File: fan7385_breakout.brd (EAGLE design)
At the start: 28.6 x 14 mm, 15 parts

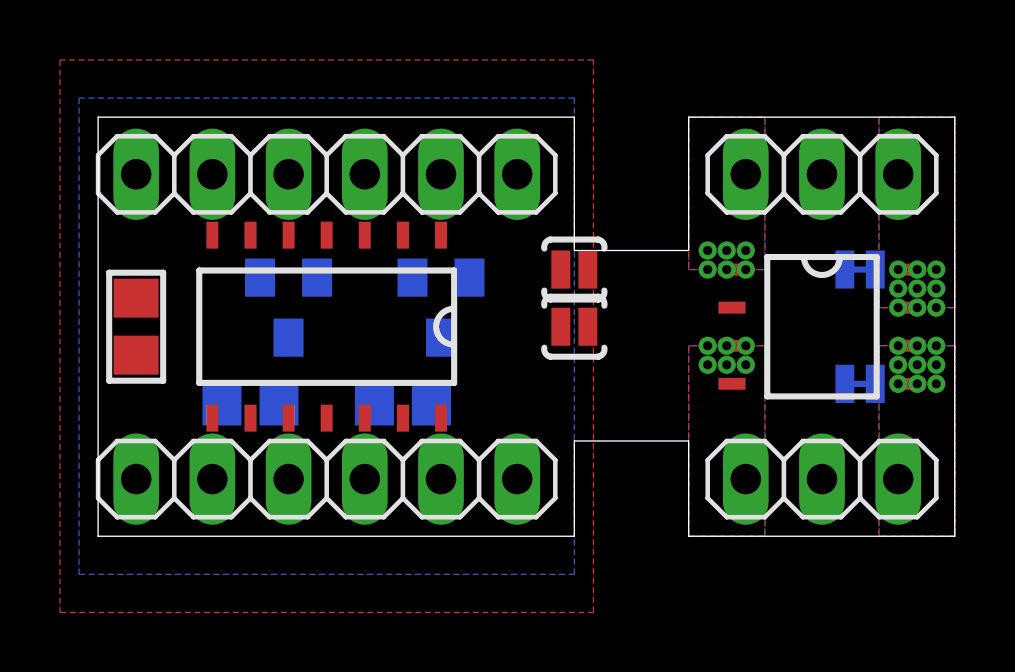
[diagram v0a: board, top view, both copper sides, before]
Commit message: a bit of manual routing, hoping it will help
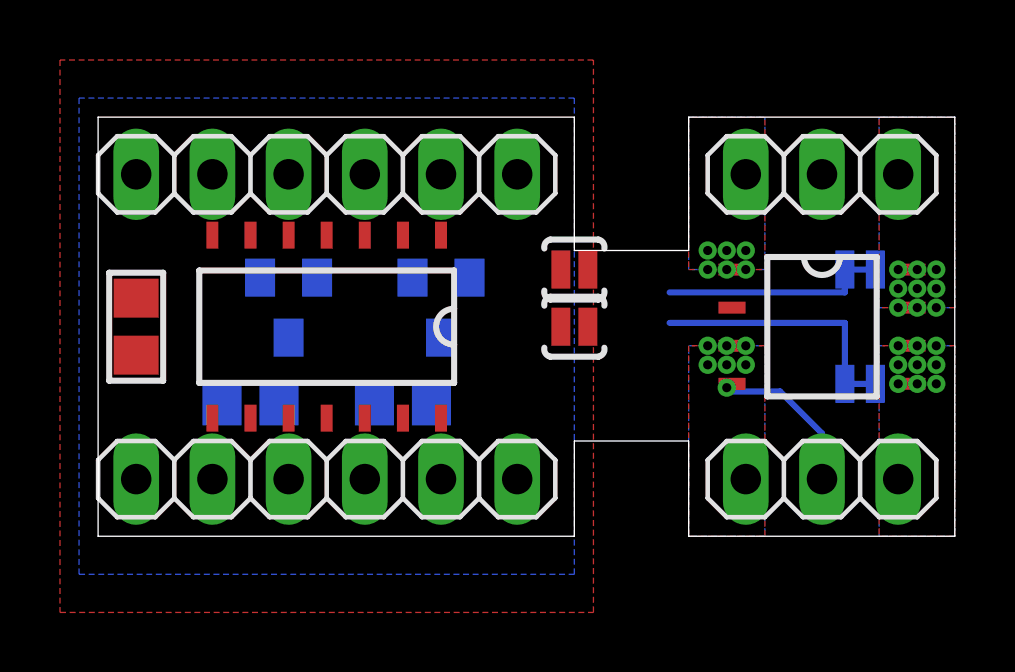
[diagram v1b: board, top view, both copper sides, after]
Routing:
- net VS2: track 0.00 -> 7.87 mm
- net VS1: track 0.00 -> 6.60 mm
- net HO2/G2: track 0.00 -> 5.56 mm, vias 0 -> 1
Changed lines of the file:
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@@
 <setting verticaltext="up"/>
 </settings>
-<grid distance="25" unitdist="mil" unit="mil" style="lines" multiple="1" display="yes" altdistance="0.025" altunitdist="inch" altunit="inch"/>
+<grid distance="5" unitdist="mil" unit="mil" style="lines" multiple="1" display="yes" altdistance="0.025" altunitdist="inch" altunit="inch"/>
 <layers>
 <layer number="1" name="Top" color="4" fill="1" visible="yes" active="yes"/>
@@
 <contactref element="JP2" pad="2"/>
 <contactref element="JP3" pad="2"/>
-<wire x1="24.13" y1="1.905" x2="21.13" y2="5.08" width="0" layer="19" extent="1-1"/>
-<wire x1="5.08" y1="3.935" x2="21.13" y2="5.08" width="0" layer="19" extent="1-1"/>
+<via x="20.955" y="4.953" extent="1-16" drill="0.3048" shape="square"/>
+<wire x1="24.13" y1="1.905" x2="24.13" y2="3.429" width="0.2032" layer="16"/>
+<wire x1="24.13" y1="3.429" x2="22.733" y2="4.826" width="0.2032" layer="16"/>
+<wire x1="22.733" y1="4.826" x2="21.082" y2="4.826" width="0.2032" layer="16"/>
+<wire x1="21.082" y1="4.826" x2="20.955" y2="4.953" width="0.2032" layer="16"/>
+<wire x1="21.13" y1="5.08" x2="21.082" y2="5.08" width="0.2032" layer="1"/>
+<wire x1="21.082" y1="5.08" x2="20.955" y2="4.953" width="0.2032" layer="1"/>
+<wire x1="5.08" y1="3.935" x2="20.955" y2="4.953" width="0" layer="19" extent="1-16"/>
 <wire x1="3.81" y1="1.905" x2="5.08" y2="3.935" width="0" layer="19" extent="1-1"/>
 </signal>
@@
 <contactref element="JP2" pad="4"/>
 <contactref element="CBOOT1" pad="1"/>
-<wire x1="9.21" y1="4.445" x2="24.892" y2="8.89" width="0" layer="19" extent="16-16"/>
+<wire x1="24.892" y1="8.89" x2="24.892" y2="8.128" width="0.2032" layer="16"/>
+<wire x1="24.892" y1="8.128" x2="19.05" y2="8.128" width="0.2032" layer="16"/>
+<wire x1="9.21" y1="4.445" x2="19.05" y2="8.128" width="0" layer="19" extent="16-16"/>
 <wire x1="8.89" y1="3.935" x2="9.21" y2="4.445" width="0" layer="19" extent="1-16"/>
 <wire x1="8.89" y1="1.905" x2="8.89" y2="3.935" width="0" layer="19" extent="1-1"/>
@@
 <contactref element="JP2" pad="1"/>
 <contactref element="CBOOT2" pad="1"/>
-<wire x1="4.13" y1="4.445" x2="24.892" y2="5.08" width="0" layer="19" extent="16-16"/>
+<wire x1="24.892" y1="5.08" x2="24.892" y2="7.112" width="0.2032" layer="16"/>
+<wire x1="24.892" y1="7.112" x2="19.05" y2="7.112" width="0.2032" layer="16"/>
+<wire x1="4.13" y1="4.445" x2="19.05" y2="7.112" width="0" layer="19" extent="16-16"/>
 <wire x1="3.81" y1="3.935" x2="4.13" y2="4.445" width="0" layer="19" extent="1-16"/>
 <wire x1="1.27" y1="1.905" x2="3.81" y2="3.935" width="0" layer="19" extent="1-1"/>

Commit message: switched to octagon pads to solve a clearance issue
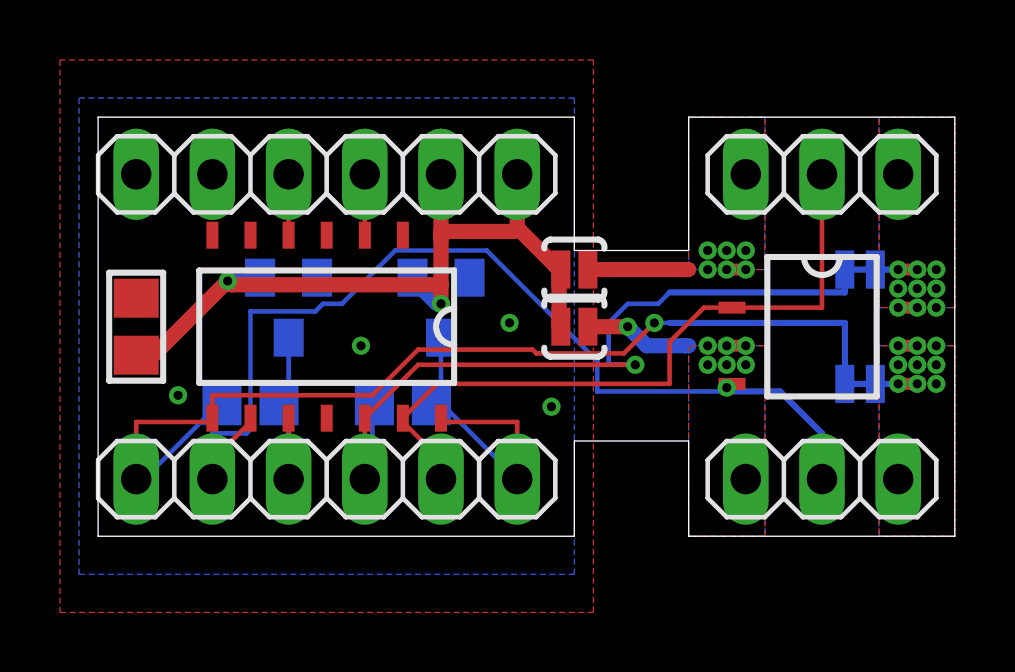
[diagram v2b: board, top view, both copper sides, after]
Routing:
- net HO2/G2: track 5.56 -> 34.3 mm
- net VDD: track 0.00 -> 26.5 mm, vias 0 -> 2
- net VS2: track 7.87 -> 33.5 mm, vias 0 -> 1
- net HO1/G1: track 0.00 -> 23.3 mm
- net VS1: track 6.60 -> 26.0 mm, vias 0 -> 1
- net VB1: track 0.00 -> 11.0 mm
- net VB2: track 0.00 -> 7.38 mm
- net S2: track 0.00 -> 3.62 mm, vias 6 -> 7
- net S1: track 0.00 -> 3.36 mm
- net IN2: track 0.00 -> 2.03 mm
- net IN1: track 0.00 -> 2.03 mm
- net D2: track 0.00 -> 0.76 mm
- net D1: track 0.00 -> 0.76 mm

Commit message: route some more stuff manually first, adjust shape for symmetry
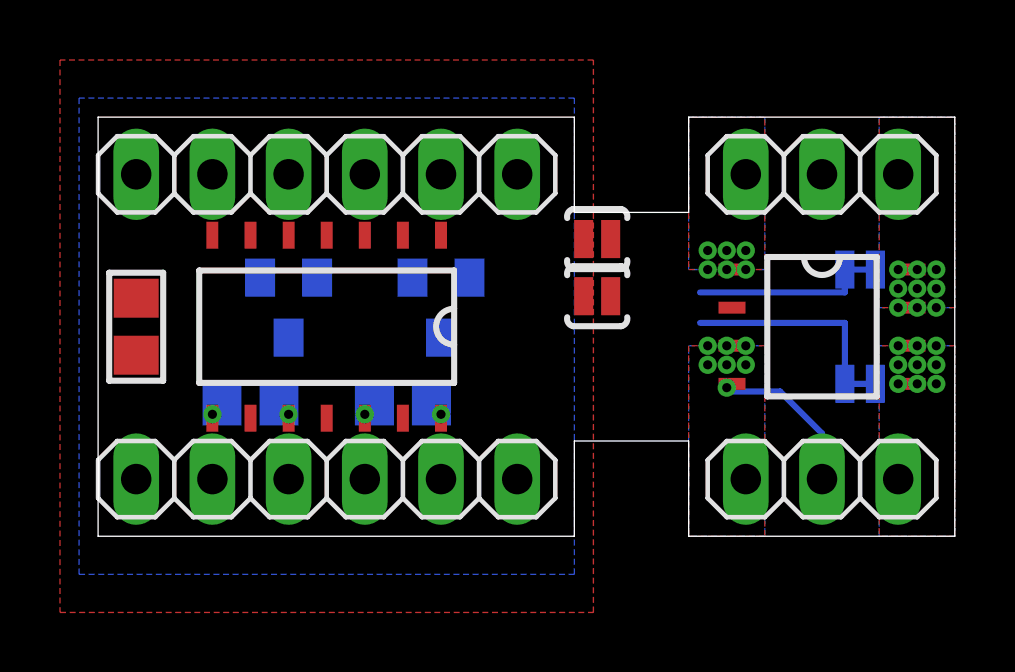
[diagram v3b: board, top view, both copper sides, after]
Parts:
- moved SJ2 1.27 mm to (16.6, 9.91)
- moved SJ1 1.27 mm to (16.6, 8.00)
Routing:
- net HO2/G2: track 34.3 -> 5.56 mm
- net VS2: track 33.5 -> 6.86 mm
- net VDD: track 26.5 -> 0.00 mm, vias 2 -> 0
- net HO1/G1: track 23.3 -> 0.00 mm
- net VS1: track 26.0 -> 5.59 mm
- net VB1: track 11.0 -> 0.00 mm, vias 0 -> 1
- net VB2: track 7.38 -> 0.00 mm, vias 0 -> 1
- net S2: track 3.62 -> 0.00 mm, vias 7 -> 6
- net S1: track 3.36 -> 0.00 mm
- net IN2: track 2.03 -> 0.00 mm
- net IN1: track 2.03 -> 0.00 mm
- net D2: track 0.76 -> 0.00 mm
- net D1: track 0.76 -> 0.00 mm
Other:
- outline, holes or cut-outs redrawn

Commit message: diffeent pin header part and 100mil spacing between pins
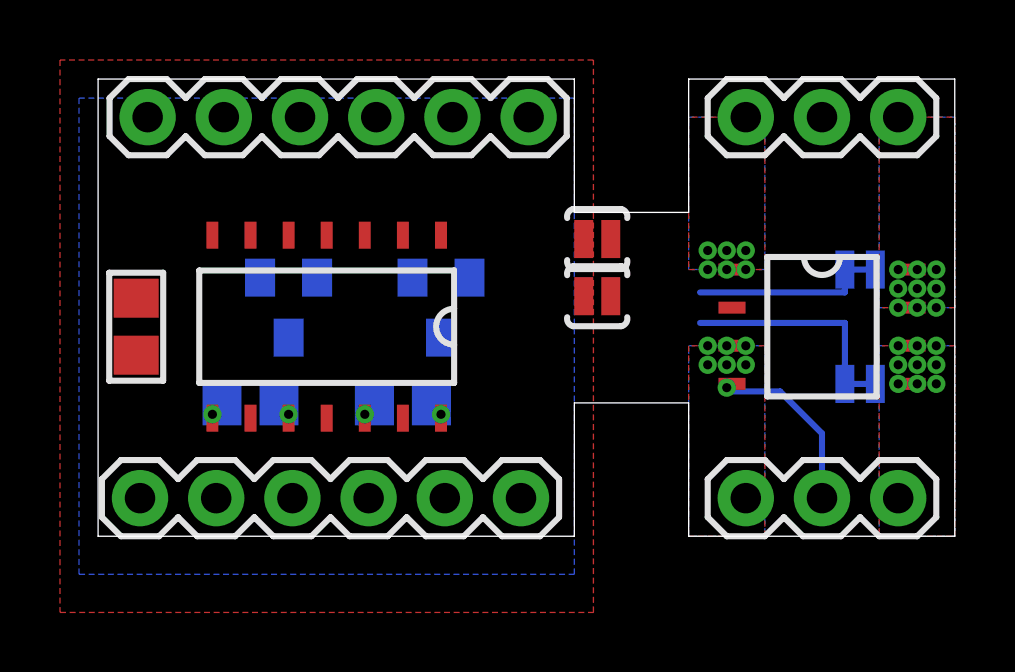
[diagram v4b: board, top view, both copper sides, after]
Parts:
- JP1, JP2: device pinhead:1X06 -> SparkFun-Connectors:1X06
- JP3, JP4: device pinhead:1X03 -> SparkFun-Connectors:1X03
- moved JP1 6.27 mm to (1.65, 14.0)
- moved JP2 6.26 mm to (1.40, 1.27)
- moved JP4 3.18 mm to (21.6, 14.0)
- moved JP3 2.62 mm to (21.6, 1.27)
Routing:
- net HO2/G2: track 5.56 -> 6.19 mm
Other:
- board size 28.6 x 14 mm -> 28.6 x 15.2 mm

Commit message: moved parts around a bit, put the bypass cap to gnd using vias
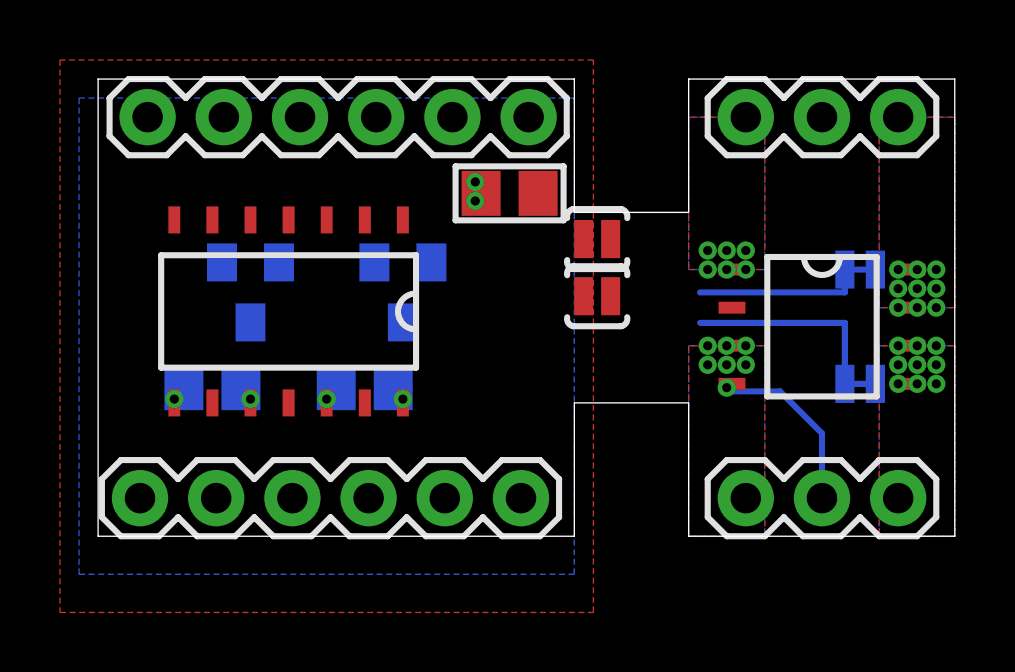
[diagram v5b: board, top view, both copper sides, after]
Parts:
- moved CVDD 13.2 mm to (13.7, 11.4), turned to 0 degrees
- moved GATEDRV 1.37 mm to (6.35, 7.49)
- moved CBOOT2 1.37 mm to (3.81, 4.95)
- moved CBOOT1 1.37 mm to (8.89, 4.95)
- moved DBOOT1 1.37 mm to (10.2, 8.13)
- moved DBOOT2 1.37 mm to (5.08, 8.13)
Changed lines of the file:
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@@
 <setting verticaltext="up"/>
 </settings>
-<grid distance="50" unitdist="mil" unit="mil" style="lines" multiple="1" display="yes" altdistance="0.025" altunitdist="inch" altunit="inch"/>
+<grid distance="5" unitdist="mil" unit="mil" style="lines" multiple="1" display="yes" altdistance="0.025" altunitdist="inch" altunit="inch"/>
 <layers>
 <layer number="1" name="Top" color="4" fill="1" visible="yes" active="yes"/>
@@
 </autorouter>
 <elements>
-<element name="GATEDRV" library="fan7385" package="SOT14" value="FAN7385" x="7.62" y="6.985" smashed="yes" rot="R270"/>
+<element name="GATEDRV" library="fan7385" package="SOT14" value="FAN7385" x="6.35" y="7.493" smashed="yes" rot="R270"/>
 <element name="FET" library="DMG9926" package="SOP8-L" value="DMG9926" x="24.13" y="6.985" smashed="yes"/>
-<element name="CBOOT1" library="microbuilder" package="0805" value="0.1uF 25V" x="10.16" y="4.445" smashed="yes" rot="MR180"/>
-<element name="CBOOT2" library="microbuilder" package="0805" value="0.1uF 25V" x="5.08" y="4.445" smashed="yes" rot="MR180"/>
-<element name="CVDD" library="microbuilder" package="0805" value="0.1uF 25V" x="1.27" y="6.985" smashed="yes" rot="R270"/>
-<element name="DBOOT2" library="microbuilder" package="SOT23-WIDE" value="" x="6.35" y="7.62" smashed="yes" rot="MR180">
-<attribute name="VALUE" x="8.255" y="8.255" size="0.4064" layer="28" ratio="10" rot="MR180"/>
+<element name="CBOOT1" library="microbuilder" package="0805" value="0.1uF 25V" x="8.89" y="4.953" smashed="yes" rot="MR180"/>
+<element name="CBOOT2" library="microbuilder" package="0805" value="0.1uF 25V" x="3.81" y="4.953" smashed="yes" rot="MR180"/>
+<element name="CVDD" library="microbuilder" package="0805" value="0.1uF 25V" x="13.716" y="11.43" smashed="yes"/>
+<element name="DBOOT2" library="microbuilder" package="SOT23-WIDE" value="" x="5.08" y="8.128" smashed="yes" rot="MR180">
+<attribute name="VALUE" x="6.985" y="8.763" size="0.4064" layer="28" ratio="10" rot="MR180"/>
 </element>
-<element name="DBOOT1" library="microbuilder" package="SOT23-WIDE" value="" x="11.43" y="7.62" smashed="yes" rot="MR180">
-<attribute name="VALUE" x="13.335" y="8.255" size="0.4064" layer="28" ratio="10" rot="MR180"/>
+<element name="DBOOT1" library="microbuilder" package="SOT23-WIDE" value="" x="10.16" y="8.128" smashed="yes" rot="MR180">
+<attribute name="VALUE" x="12.065" y="8.763" size="0.4064" layer="28" ratio="10" rot="MR180"/>
 </element>
 <element name="SJ1" library="SparkFun-Passives" package="SJ_2S-NO" value="SOLDERJUMPERNO" x="16.637" y="8.001" smashed="yes"/>
@@
 <contactref element="JP1" pad="2"/>
 <contactref element="JP1" pad="1"/>
+<via x="12.573" y="11.811" extent="1-16" drill="0.3048" shape="square"/>
+<via x="12.573" y="11.176" extent="1-16" drill="0.3048" shape="square"/>
 </signal>
 <signal name="VDD" class="2">
@@
 <contactref element="JP1" pad="6"/>
 <contactref element="JP1" pad="5"/>
+<wire x1="14.666" y1="11.43" x2="14.351" y2="13.97" width="0" layer="19" extent="1-1"/>
+<wire x1="16.187" y1="9.906" x2="14.666" y2="11.43" width="0" layer="19" extent="1-1"/>
+<wire x1="16.187" y1="8.001" x2="16.187" y2="9.906" width="0" layer="19" extent="1-1"/>
 <wire x1="11.811" y1="13.97" x2="14.351" y2="13.97" width="0" layer="19" extent="1-1"/>
-<wire x1="11.43" y1="10.035" x2="11.811" y2="13.97" width="0" layer="19" extent="1-1"/>
-<wire x1="10.48" y1="8.62" x2="11.43" y2="10.035" width="0" layer="19" extent="1-16"/>
-<wire x1="16.187" y1="9.906" x2="14.351" y2="13.97" width="0" layer="19" extent="1-1"/>
-<wire x1="16.187" y1="8.001" x2="16.187" y2="9.906" width="0" layer="19" extent="1-1"/>
-<wire x1="5.4" y1="8.62" x2="10.48" y2="8.62" width="0" layer="19" extent="16-16"/>
-<wire x1="1.27" y1="6.035" x2="5.4" y2="8.62" width="0" layer="19" extent="1-16"/>
+<wire x1="10.16" y1="10.543" x2="11.811" y2="13.97" width="0" layer="19" extent="1-1"/>
+<wire x1="9.21" y1="9.128" x2="10.16" y2="10.543" width="0" layer="19" extent="1-16"/>
+<wire x1="4.13" y1="9.128" x2="9.21" y2="9.128" width="0" layer="19" extent="16-16"/>
 </signal>
 <signal name="S1" class="2">
@@
 <contactref element="GATEDRV" pad="3"/>
 <contactref element="JP1" pad="4"/>
-<wire x1="8.89" y1="10.035" x2="9.271" y2="13.97" width="0" layer="19" extent="1-1"/>
+<wire x1="7.62" y1="10.543" x2="9.271" y2="13.97" width="0" layer="19" extent="1-1"/>
 </signal>
 <signal name="IN2">
 <contactref element="GATEDRV" pad="5"/>
 <contactref element="JP1" pad="3"/>
-<wire x1="6.35" y1="10.035" x2="6.731" y2="13.97" width="0" layer="19" extent="1-1"/>
+<wire x1="5.08" y1="10.543" x2="6.731" y2="13.97" width="0" layer="19" extent="1-1"/>
 </signal>
 <signal name="HO1/G1">
@@
 <wire x1="21.13" y1="7.62" x2="24.13" y2="13.97" width="0" layer="19" extent="1-1"/>
 <wire x1="11.557" y1="1.27" x2="21.13" y2="7.62" width="0" layer="19" extent="1-1"/>
-<wire x1="10.16" y1="3.935" x2="11.557" y2="1.27" width="0" layer="19" extent="1-1"/>
+<wire x1="8.89" y1="4.443" x2="11.557" y2="1.27" width="0" layer="19" extent="1-1"/>
 </signal>
 <signal name="HO2/G2">
@@
 <contactref element="JP2" pad="2"/>
 <contactref element="JP3" pad="2"/>
-<wire x1="5.08" y1="3.935" x2="20.955" y2="4.953" width="0" layer="19" extent="1-16"/>
-<wire x1="3.937" y1="1.27" x2="5.08" y2="3.935" width="0" layer="19" extent="1-1"/>
 <wire x1="24.13" y1="3.429" x2="24.13" y2="1.27" width="0.2032" layer="16"/>
+<wire x1="3.81" y1="4.443" x2="20.955" y2="4.953" width="0" layer="19" extent="1-1"/>
+<wire x1="3.937" y1="1.27" x2="3.81" y2="4.443" width="0" layer="19" extent="1-1"/>
 </signal>
 <signal name="VB1">
@@
 <contactref element="CBOOT1" pad="2"/>
 <contactref element="DBOOT1" pad="3"/>
-<via x="11.43" y="4.064" extent="1-16" drill="0.3048" shape="square"/>
+<via x="10.16" y="4.572" extent="1-16" drill="0.3048" shape="square"/>
 <contactref element="JP2" pad="6"/>
-<wire x1="11.11" y1="4.445" x2="11.43" y2="6.62" width="0" layer="19" extent="16-16"/>
-<wire x1="11.43" y1="4.064" x2="11.11" y2="4.445" width="0" layer="19" extent="16-16"/>
-<wire x1="11.43" y1="3.935" x2="11.43" y2="4.064" width="0" layer="19" extent="1-1"/>
-<wire x1="14.097" y1="1.27" x2="11.43" y2="3.935" width="0" layer="19" extent="1-1"/>
+<wire x1="9.84" y1="4.953" x2="10.16" y2="7.128" width="0" layer="19" extent="16-16"/>
+<wire x1="10.16" y1="4.572" x2="9.84" y2="4.953" width="0" layer="19" extent="16-16"/>
+<wire x1="10.16" y1="4.443" x2="10.16" y2="4.572" width="0" layer="19" extent="1-1"/>
+<wire x1="14.097" y1="1.27" x2="10.16" y2="4.443" width="0" layer="19" extent="1-1"/>
 </signal>
 <signal name="VB2">
@@
 <contactref element="CBOOT2" pad="2"/>
 <contactref element="DBOOT2" pad="3"/>
-<via x="6.35" y="4.064" extent="1-16" drill="0.3048" shape="square"/>
+<via x="5.08" y="4.572" extent="1-16" drill="0.3048" shape="square"/>
 <contactref element="JP2" pad="3"/>
-<wire x1="6.03" y1="4.445" x2="6.35" y2="6.62" width="0" layer="19" extent="16-16"/>
-<wire x1="6.35" y1="4.064" x2="6.03" y2="4.445" width="0" layer="19" extent="16-16"/>
-<wire x1="6.35" y1="3.935" x2="6.35" y2="4.064" width="0" layer="19" extent="1-1"/>
-<wire x1="6.477" y1="1.27" x2="6.35" y2="3.935" width="0" layer="19" extent="1-1"/>
+<wire x1="4.76" y1="4.953" x2="5.08" y2="7.128" width="0" layer="19" extent="16-16"/>
+<wire x1="5.08" y1="4.572" x2="4.76" y2="4.953" width="0" layer="19" extent="16-16"/>
+<wire x1="5.08" y1="4.443" x2="5.08" y2="4.572" width="0" layer="19" extent="1-1"/>
+<wire x1="6.477" y1="1.27" x2="5.08" y2="4.443" width="0" layer="19" extent="1-1"/>
 </signal>
 <signal name="D2" class="2">
@@
 <wire x1="24.892" y1="8.89" x2="24.892" y2="8.128" width="0.2032" layer="16"/>
 <wire x1="24.892" y1="8.128" x2="20.066" y2="8.128" width="0.2032" layer="16"/>
-<via x="8.89" y="4.064" extent="1-16" drill="0.3048" shape="square"/>
+<via x="7.62" y="4.572" extent="1-16" drill="0.3048" shape="square"/>
 <contactref element="JP2" pad="4"/>
-<wire x1="9.21" y1="4.445" x2="20.066" y2="8.128" width="0" layer="19" extent="16-16"/>
-<wire x1="8.89" y1="4.064" x2="9.21" y2="4.445" width="0" layer="19" extent="16-16"/>
-<wire x1="8.89" y1="3.935" x2="8.89" y2="4.064" width="0" layer="19" extent="1-1"/>
-<wire x1="9.017" y1="1.27" x2="8.89" y2="3.935" width="0" layer="19" extent="1-1"/>
+<wire x1="7.94" y1="4.953" x2="20.066" y2="8.128" width="0" layer="19" extent="16-16"/>
+<wire x1="7.62" y1="4.572" x2="7.94" y2="4.953" width="0" layer="19" extent="16-16"/>
+<wire x1="7.62" y1="4.443" x2="7.62" y2="4.572" width="0" layer="19" extent="1-1"/>
+<wire x1="9.017" y1="1.27" x2="7.62" y2="4.443" width="0" layer="19" extent="1-1"/>
 </signal>
 <signal name="VS2">
@@
 <wire x1="24.892" y1="5.08" x2="24.892" y2="7.112" width="0.2032" layer="16"/>
 <wire x1="24.892" y1="7.112" x2="20.066" y2="7.112" width="0.2032" layer="16"/>
-<via x="3.81" y="4.064" extent="1-16" drill="0.3048" shape="square"/>
+<via x="2.54" y="4.572" extent="1-16" drill="0.3048" shape="square"/>
 <contactref element="JP2" pad="1"/>
-<wire x1="4.13" y1="4.445" x2="20.066" y2="7.112" width="0" layer="19" extent="16-16"/>
-<wire x1="3.81" y1="4.064" x2="4.13" y2="4.445" width="0" layer="19" extent="16-16"/>
-<wire x1="3.81" y1="3.935" x2="3.81" y2="4.064" width="0" layer="19" extent="1-1"/>
-<wire x1="1.397" y1="1.27" x2="3.81" y2="3.935" width="0" layer="19" extent="1-1"/>
+<wire x1="2.86" y1="4.953" x2="20.066" y2="7.112" width="0" layer="19" extent="16-16"/>
+<wire x1="2.54" y1="4.572" x2="2.86" y2="4.953" width="0" layer="19" extent="16-16"/>
+<wire x1="2.54" y1="4.443" x2="2.54" y2="4.572" width="0" layer="19" extent="1-1"/>
+<wire x1="1.397" y1="1.27" x2="2.54" y2="4.443" width="0" layer="19" extent="1-1"/>
 </signal>
 </signals>
